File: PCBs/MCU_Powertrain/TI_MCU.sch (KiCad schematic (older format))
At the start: 50 parts, among them SW1 SW_Push, SW2 SW_Push, U5 TMS320F28027F, U6 SN74LVC2G07, U7 SN74LVC2G07

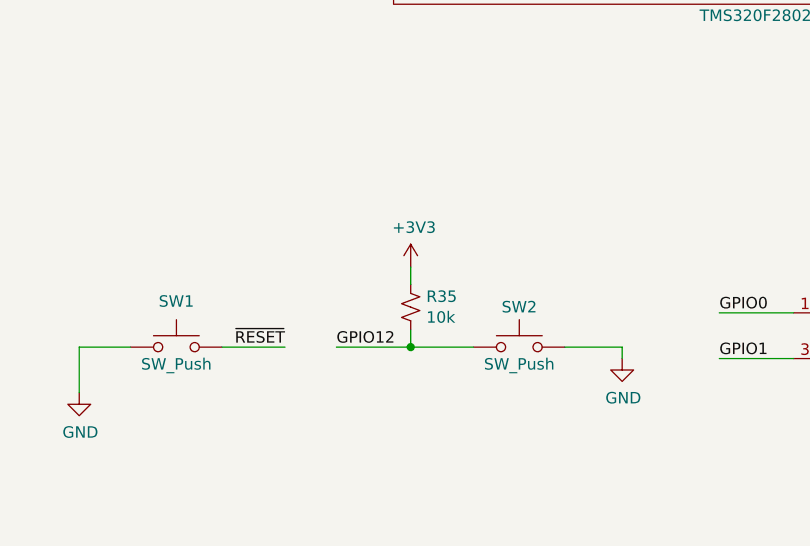
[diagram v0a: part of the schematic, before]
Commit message: Small Tweaks
- Removed double CAN int pullup
- Double checked overall schematic
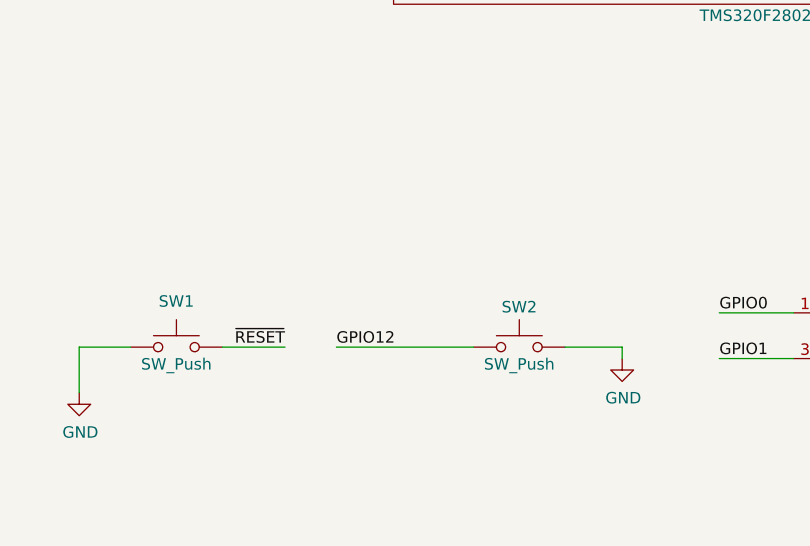
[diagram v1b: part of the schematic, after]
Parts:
- removed R35: 10k, Resistors_SMD:R_0805, symbol Device:R_Small_US
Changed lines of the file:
@@
 	4575 5525 4825 5525
-$Comp
-L power:+3V3 #PWR0162
-U 1 1 5E2D1E69
-P 3900 5175
-F 0 "#PWR0162" H 3900 5025 50  0001 C CNN
-F 1 "+3V3" H 3915 5348 50  0000 C CNN
-F 2 "" H 3900 5175 50  0001 C CNN
-F 3 "" H 3900 5175 50  0001 C CNN
-	1    3900 5175
-	1    0    0    -1
-$EndComp
-$Comp
-L Device:R_Small_US R35
-U 1 1 5E2D5182
-P 3900 5350
-F 0 "R35" H 3968 5396 50  0000 L CNN
-F 1 "10k" H 3968 5305 50  0000 L CNN
-F 2 "Resistors_SMD:R_0805" H 3900 5350 50  0001 C CNN
-F 3 "~" H 3900 5350 50  0001 C CNN
-F 4 "311-10.0KCRCT-ND" H 3900 5350 50  0001 C CNN "Digikey"
-	1    3900 5350
-	1    0    0    -1
-$EndComp
 $Comp
 L power:GND #PWR0163
@@
 Text Label 9875 4825 0    50   ~ 0
 GPIO12
-Wire Wire Line
-	3575 5525 3900 5525
-Wire Wire Line
-	3900 5450 3900 5525
-Connection ~ 3900 5525
-Wire Wire Line
-	3900 5525 4175 5525
-Wire Wire Line
-	3900 5250 3900 5175
 Text Label 9875 4425 0    50   ~ 0
 GPIO32
@@
 	1    0    0    -1
 $EndComp
+Wire Wire Line
+	3575 5525 4175 5525
 $EndSCHEMATC

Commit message: Initial Layout, 3D Models, 0402s
- Changed C2, C4, C9, C16, C18 to 0402
- Some intial layout
- All 3D models added
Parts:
- SW1, SW2: Digikey (none) -> CKN9112CT-ND
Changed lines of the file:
@@
 F 2 "Buttons_Switches_SMD:SW_SPST_EVQQ2" H 2875 5725 50  0001 C CNN
 F 3 "~" H 2875 5725 50  0001 C CNN
+F 4 "CKN9112CT-ND" H 2875 5525 50  0001 C CNN "Digikey"
 	1    2875 5525
 	1    0    0    -1
@@
 F 2 "Buttons_Switches_SMD:SW_SPST_EVQQ2" H 4375 5725 50  0001 C CNN
 F 3 "~" H 4375 5725 50  0001 C CNN
+F 4 "CKN9112CT-ND" H 4375 5525 50  0001 C CNN "Digikey"
 	1    4375 5525
 	1    0    0    -1

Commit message: More Layout + Schematic
- Fixed small issue with net labels, ISEN labels were not seperated on the DRV sheet.
- More layout
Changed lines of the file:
@@
 Wire Wire Line
 	3725 3225 3400 3225
-Wire Wire Line
-	3725 3325 3400 3325
 Text Label 3400 3025 0    50   ~ 0
 ADCINB3
@@
 Text Label 3400 3225 0    50   ~ 0
 ADCINB6
-Text Label 3400 3325 0    50   ~ 0
-ADCINB7
 Wire Wire Line
 	3725 3425 3400 3425
@@
 Wire Wire Line
 	3575 5525 4175 5525
+Text Label 3400 3325 0    50   ~ 0
+ADCINB7
+Wire Wire Line
+	3400 3325 3725 3325
 $EndSCHEMATC

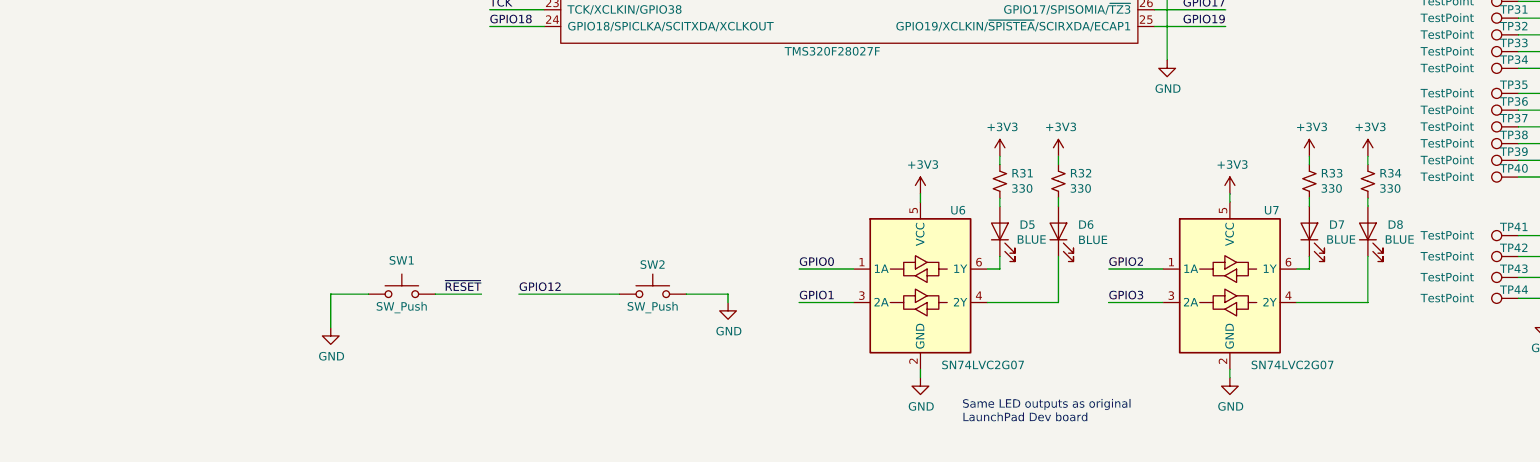
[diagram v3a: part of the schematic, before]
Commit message: Initial Layout
- Full initial layout complete, can probably shrink the board further as routing is complete
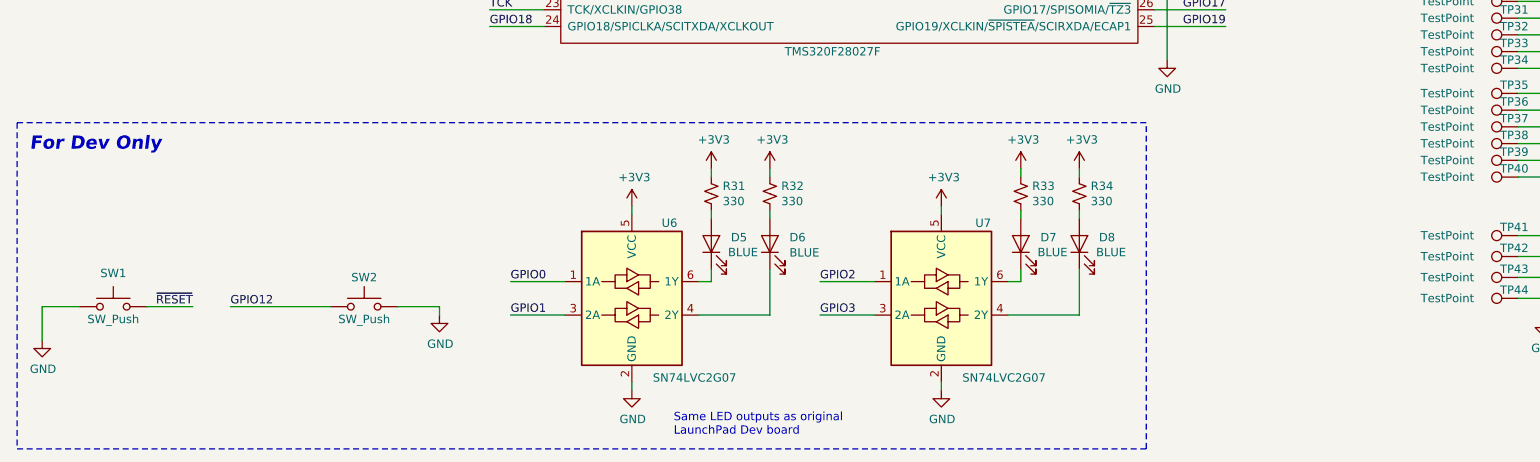
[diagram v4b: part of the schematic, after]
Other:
- note added: "For Dev Only"
- moved on the sheet: D5, D6, D7, D8, R31, R32, R33, R34, SW1, SW2, U6, U7

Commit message: Routing
- Routed most of DRV and TI chips
- FETs are done
- Added board outline
- Added power and ground planes
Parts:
- TP22, TP23, TP24, TP25, TP26, TP27, TP28, TP29, TP30, TP31, TP32, TP33, TP34, TP35, TP36, TP37, TP38, TP39, TP40, TP41, TP42, TP43, TP44: footprint Testpoints:TestPoint_Loop_D1.80mm_Drill1.0mm_Beaded -> MCU_Powertrain:TestPoint_Loop_D1.80mm_Drill1.0mm_Beaded
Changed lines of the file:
@@
 F 0 "TP29" V 9600 3700 50  0000 C CNN
 F 1 "TestPoint" V 9550 4100 50  0000 C CNN
-F 2 "Testpoints:TestPoint_Loop_D1.80mm_Drill1.0mm_Beaded" H 9750 3675 50  0001 C CNN
+F 2 "MCU_Powertrain:TestPoint_Loop_D1.80mm_Drill1.0mm_Beaded" H 9750 3675 50  0001 C CNN
 F 3 "~" H 9750 3675 50  0001 C CNN
 F 4 "36-5116-ND" V 9550 3675 50  0001 C CNN "Digikey"
@@
 F 0 "TP30" V 9600 3800 50  0000 C CNN
 F 1 "TestPoint" V 9550 4200 50  0000 C CNN
-F 2 "Testpoints:TestPoint_Loop_D1.80mm_Drill1.0mm_Beaded" H 9750 3775 50  0001 C CNN
+F 2 "MCU_Powertrain:TestPoint_Loop_D1.80mm_Drill1.0mm_Beaded" H 9750 3775 50  0001 C CNN
 F 3 "~" H 9750 3775 50  0001 C CNN
 F 4 "36-5116-ND" V 9550 3775 50  0001 C CNN "Digikey"
@@
 F 0 "TP22" V 9600 2950 50  0000 C CNN
 F 1 "TestPoint" V 9550 3350 50  0000 C CNN
-F 2 "Testpoints:TestPoint_Loop_D1.80mm_Drill1.0mm_Beaded" H 9750 2925 50  0001 C CNN
+F 2 "MCU_Powertrain:TestPoint_Loop_D1.80mm_Drill1.0mm_Beaded" H 9750 2925 50  0001 C CNN
 F 3 "~" H 9750 2925 50  0001 C CNN
 F 4 "36-5117-ND" V 9550 2925 50  0001 C CNN "Digikey"
@@
 F 0 "TP41" V 9600 5200 50  0000 C CNN
 F 1 "TestPoint" V 9550 5600 50  0000 C CNN
-F 2 "Testpoints:TestPoint_Loop_D1.80mm_Drill1.0mm_Beaded" H 9750 5175 50  0001 C CNN
+F 2 "MCU_Powertrain:TestPoint_Loop_D1.80mm_Drill1.0mm_Beaded" H 9750 5175 50  0001 C CNN
 F 3 "~" H 9750 5175 50  0001 C CNN
 F 4 "36-5001-ND" V 9550 5175 50  0001 C CNN "Digikey"
@@
 F 0 "TP42" V 9600 5325 50  0000 C CNN
 F 1 "TestPoint" V 9550 5725 50  0000 C CNN
-F 2 "Testpoints:TestPoint_Loop_D1.80mm_Drill1.0mm_Beaded" H 9750 5300 50  0001 C CNN
+F 2 "MCU_Powertrain:TestPoint_Loop_D1.80mm_Drill1.0mm_Beaded" H 9750 5300 50  0001 C CNN
 F 3 "~" H 9750 5300 50  0001 C CNN
 F 4 "36-5001-ND" V 9550 5300 50  0001 C CNN "Digikey"
@@
 F 0 "TP43" V 9600 5450 50  0000 C CNN
 F 1 "TestPoint" V 9550 5850 50  0000 C CNN
-F 2 "Testpoints:TestPoint_Loop_D1.80mm_Drill1.0mm_Beaded" H 9750 5425 50  0001 C CNN
+F 2 "MCU_Powertrain:TestPoint_Loop_D1.80mm_Drill1.0mm_Beaded" H 9750 5425 50  0001 C CNN
 F 3 "~" H 9750 5425 50  0001 C CNN
 F 4 "36-5001-ND" V 9550 5425 50  0001 C CNN "Digikey"
@@
 F 0 "TP44" V 9600 5575 50  0000 C CNN
 F 1 "TestPoint" V 9550 5975 50  0000 C CNN
-F 2 "Testpoints:TestPoint_Loop_D1.80mm_Drill1.0mm_Beaded" H 9750 5550 50  0001 C CNN
+F 2 "MCU_Powertrain:TestPoint_Loop_D1.80mm_Drill1.0mm_Beaded" H 9750 5550 50  0001 C CNN
 F 3 "~" H 9750 5550 50  0001 C CNN
 F 4 "36-5001-ND" V 9550 5550 50  0001 C CNN "Digikey"
@@
 F 0 "TP31" V 9600 3900 50  0000 C CNN
 F 1 "TestPoint" V 9550 4300 50  0000 C CNN
-F 2 "Testpoints:TestPoint_Loop_D1.80mm_Drill1.0mm_Beaded" H 9750 3875 50  0001 C CNN
+F 2 "MCU_Powertrain:TestPoint_Loop_D1.80mm_Drill1.0mm_Beaded" H 9750 3875 50  0001 C CNN
 F 3 "~" H 9750 3875 50  0001 C CNN
 F 4 "36-5116-ND" V 9550 3875 50  0001 C CNN "Digikey"
@@
 F 0 "TP32" V 9600 4000 50  0000 C CNN
 F 1 "TestPoint" V 9550 4400 50  0000 C CNN
-F 2 "Testpoints:TestPoint_Loop_D1.80mm_Drill1.0mm_Beaded" H 9750 3975 50  0001 C CNN
+F 2 "MCU_Powertrain:TestPoint_Loop_D1.80mm_Drill1.0mm_Beaded" H 9750 3975 50  0001 C CNN
 F 3 "~" H 9750 3975 50  0001 C CNN
 F 4 "36-5116-ND" V 9550 3975 50  0001 C CNN "Digikey"
@@
 F 0 "TP33" V 9600 4100 50  0000 C CNN
 F 1 "TestPoint" V 9550 4500 50  0000 C CNN
-F 2 "Testpoints:TestPoint_Loop_D1.80mm_Drill1.0mm_Beaded" H 9750 4075 50  0001 C CNN
+F 2 "MCU_Powertrain:TestPoint_Loop_D1.80mm_Drill1.0mm_Beaded" H 9750 4075 50  0001 C CNN
 F 3 "~" H 9750 4075 50  0001 C CNN
 F 4 "36-5116-ND" V 9550 4075 50  0001 C CNN "Digikey"
@@
 F 0 "TP34" V 9600 4200 50  0000 C CNN
 F 1 "TestPoint" V 9550 4600 50  0000 C CNN
-F 2 "Testpoints:TestPoint_Loop_D1.80mm_Drill1.0mm_Beaded" H 9750 4175 50  0001 C CNN
+F 2 "MCU_Powertrain:TestPoint_Loop_D1.80mm_Drill1.0mm_Beaded" H 9750 4175 50  0001 C CNN
 F 3 "~" H 9750 4175 50  0001 C CNN
 F 4 "36-5116-ND" V 9550 4175 50  0001 C CNN "Digikey"
@@
 F 0 "TP35" V 9600 4350 50  0000 C CNN
 F 1 "TestPoint" V 9550 4750 50  0000 C CNN
-F 2 "Testpoints:TestPoint_Loop_D1.80mm_Drill1.0mm_Beaded" H 9750 4325 50  0001 C CNN
+F 2 "MCU_Powertrain:TestPoint_Loop_D1.80mm_Drill1.0mm_Beaded" H 9750 4325 50  0001 C CNN
 F 3 "~" H 9750 4325 50  0001 C CNN
 F 4 "36-5119-ND" V 9550 4325 50  0001 C CNN "Digikey"
@@
 F 0 "TP36" V 9600 4450 50  0000 C CNN
 F 1 "TestPoint" V 9550 4850 50  0000 C CNN
-F 2 "Testpoints:TestPoint_Loop_D1.80mm_Drill1.0mm_Beaded" H 9750 4425 50  0001 C CNN
+F 2 "MCU_Powertrain:TestPoint_Loop_D1.80mm_Drill1.0mm_Beaded" H 9750 4425 50  0001 C CNN
 F 3 "~" H 9750 4425 50  0001 C CNN
 F 4 "36-5119-ND" V 9550 4425 50  0001 C CNN "Digikey"
@@
 F 0 "TP37" V 9600 4550 50  0000 C CNN
 F 1 "TestPoint" V 9550 4950 50  0000 C CNN
-F 2 "Testpoints:TestPoint_Loop_D1.80mm_Drill1.0mm_Beaded" H 9750 4525 50  0001 C CNN
+F 2 "MCU_Powertrain:TestPoint_Loop_D1.80mm_Drill1.0mm_Beaded" H 9750 4525 50  0001 C CNN
 F 3 "~" H 9750 4525 50  0001 C CNN
 F 4 "36-5119-ND" V 9550 4525 50  0001 C CNN "Digikey"
@@
 F 0 "TP38" V 9600 4650 50  0000 C CNN
 F 1 "TestPoint" V 9550 5050 50  0000 C CNN
-F 2 "Testpoints:TestPoint_Loop_D1.80mm_Drill1.0mm_Beaded" H 9750 4625 50  0001 C CNN
+F 2 "MCU_Powertrain:TestPoint_Loop_D1.80mm_Drill1.0mm_Beaded" H 9750 4625 50  0001 C CNN
 F 3 "~" H 9750 4625 50  0001 C CNN
 F 4 "36-5119-ND" V 9550 4625 50  0001 C CNN "Digikey"
@@
 F 0 "TP39" V 9600 4750 50  0000 C CNN
 F 1 "TestPoint" V 9550 5150 50  0000 C CNN
-F 2 "Testpoints:TestPoint_Loop_D1.80mm_Drill1.0mm_Beaded" H 9750 4725 50  0001 C CNN
+F 2 "MCU_Powertrain:TestPoint_Loop_D1.80mm_Drill1.0mm_Beaded" H 9750 4725 50  0001 C CNN
 F 3 "~" H 9750 4725 50  0001 C CNN
 F 4 "36-5119-ND" V 9550 4725 50  0001 C CNN "Digikey"
@@
 F 0 "TP40" V 9600 4850 50  0000 C CNN
 F 1 "TestPoint" V 9550 5250 50  0000 C CNN
-F 2 "Testpoints:TestPoint_Loop_D1.80mm_Drill1.0mm_Beaded" H 9750 4825 50  0001 C CNN
+F 2 "MCU_Powertrain:TestPoint_Loop_D1.80mm_Drill1.0mm_Beaded" H 9750 4825 50  0001 C CNN
 F 3 "~" H 9750 4825 50  0001 C CNN
 F 4 "36-5119-ND" V 9550 4825 50  0001 C CNN "Digikey"
@@
 F 0 "TP23" V 9600 3050 50  0000 C CNN
 F 1 "TestPoint" V 9550 3450 50  0000 C CNN
-F 2 "Testpoints:TestPoint_Loop_D1.80mm_Drill1.0mm_Beaded" H 9750 3025 50  0001 C CNN
+F 2 "MCU_Powertrain:TestPoint_Loop_D1.80mm_Drill1.0mm_Beaded" H 9750 3025 50  0001 C CNN
 F 3 "~" H 9750 3025 50  0001 C CNN
 F 4 "36-5117-ND" V 9550 3025 50  0001 C CNN "Digikey"
@@
 F 0 "TP24" V 9600 3150 50  0000 C CNN
 F 1 "TestPoint" V 9550 3550 50  0000 C CNN
-F 2 "Testpoints:TestPoint_Loop_D1.80mm_Drill1.0mm_Beaded" H 9750 3125 50  0001 C CNN
+F 2 "MCU_Powertrain:TestPoint_Loop_D1.80mm_Drill1.0mm_Beaded" H 9750 3125 50  0001 C CNN
 F 3 "~" H 9750 3125 50  0001 C CNN
 F 4 "36-5117-ND" V 9550 3125 50  0001 C CNN "Digikey"
@@
 F 0 "TP25" V 9600 3250 50  0000 C CNN
 F 1 "TestPoint" V 9550 3650 50  0000 C CNN
-F 2 "Testpoints:TestPoint_Loop_D1.80mm_Drill1.0mm_Beaded" H 9750 3225 50  0001 C CNN
+F 2 "MCU_Powertrain:TestPoint_Loop_D1.80mm_Drill1.0mm_Beaded" H 9750 3225 50  0001 C CNN
 F 3 "~" H 9750 3225 50  0001 C CNN
 F 4 "36-5117-ND" V 9550 3225 50  0001 C CNN "Digikey"
@@
 F 0 "TP26" V 9600 3350 50  0000 C CNN
 F 1 "TestPoint" V 9550 3750 50  0000 C CNN
-F 2 "Testpoints:TestPoint_Loop_D1.80mm_Drill1.0mm_Beaded" H 9750 3325 50  0001 C CNN
+F 2 "MCU_Powertrain:TestPoint_Loop_D1.80mm_Drill1.0mm_Beaded" H 9750 3325 50  0001 C CNN
 F 3 "~" H 9750 3325 50  0001 C CNN
 F 4 "36-5117-ND" V 9550 3325 50  0001 C CNN "Digikey"
@@
 F 0 "TP27" V 9600 3450 50  0000 C CNN
 F 1 "TestPoint" V 9550 3850 50  0000 C CNN
-F 2 "Testpoints:TestPoint_Loop_D1.80mm_Drill1.0mm_Beaded" H 9750 3425 50  0001 C CNN
+F 2 "MCU_Powertrain:TestPoint_Loop_D1.80mm_Drill1.0mm_Beaded" H 9750 3425 50  0001 C CNN
 F 3 "~" H 9750 3425 50  0001 C CNN
 F 4 "36-5117-ND" V 9550 3425 50  0001 C CNN "Digikey"
@@
 F 0 "TP28" V 9600 3550 50  0000 C CNN
 F 1 "TestPoint" V 9550 3950 50  0000 C CNN
-F 2 "Testpoints:TestPoint_Loop_D1.80mm_Drill1.0mm_Beaded" H 9750 3525 50  0001 C CNN
+F 2 "MCU_Powertrain:TestPoint_Loop_D1.80mm_Drill1.0mm_Beaded" H 9750 3525 50  0001 C CNN
 F 3 "~" H 9750 3525 50  0001 C CNN
 F 4 "36-5117-ND" V 9550 3525 50  0001 C CNN "Digikey"
